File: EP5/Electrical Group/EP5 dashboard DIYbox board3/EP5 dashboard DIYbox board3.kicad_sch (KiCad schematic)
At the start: 9 parts, among them J1 suspension left, J2 suspension right, J3 MCU, J4 wheel left, J5 wheel right

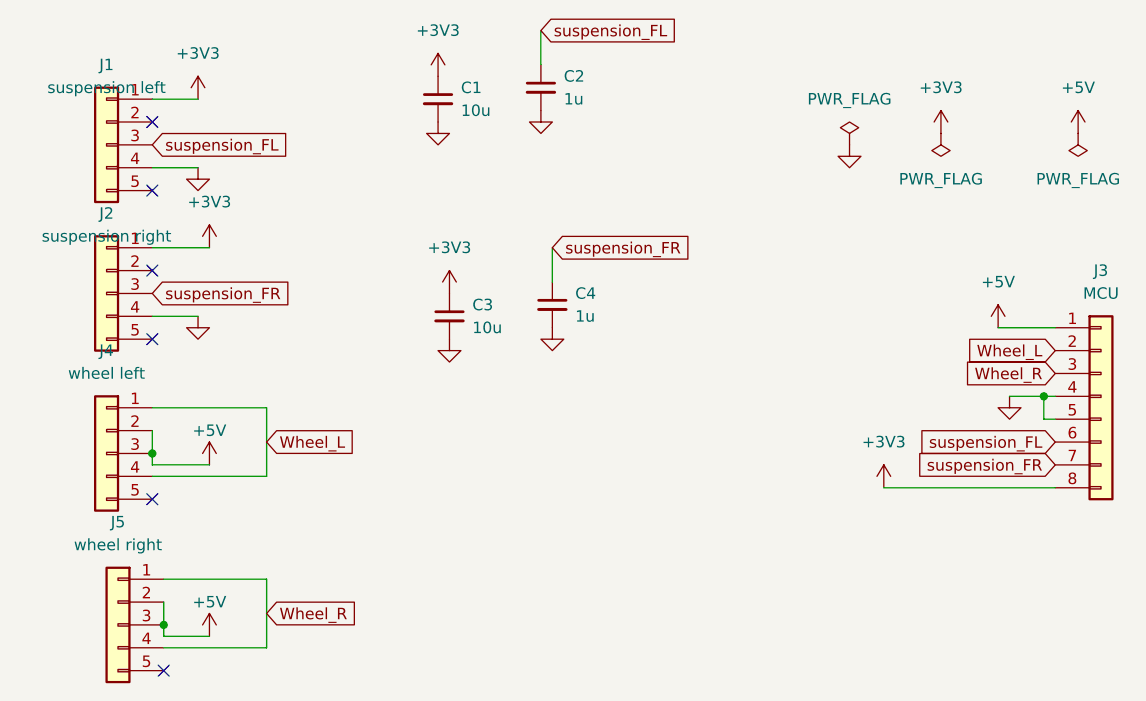
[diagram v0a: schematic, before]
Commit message: update dashboard boards after Tsou's review
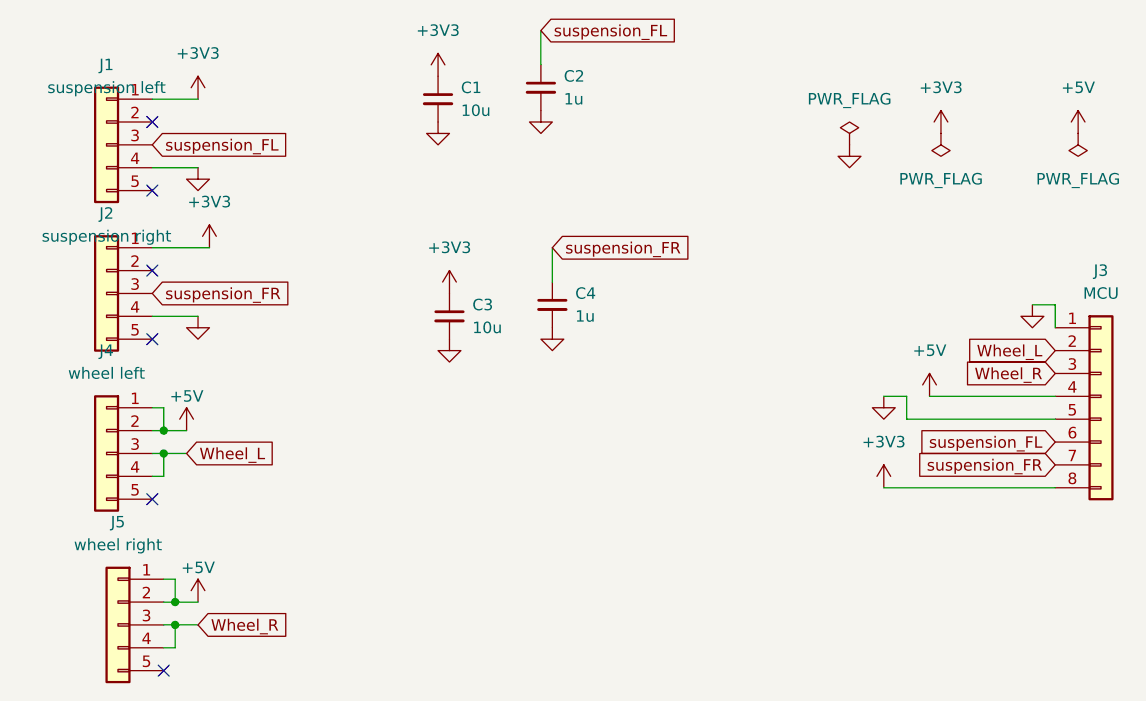
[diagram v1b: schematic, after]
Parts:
- C1, C2, C3, C4: footprint Capacitor_SMD:C_0805_2012Metric -> Capacitor_Tantalum_SMD:CP_EIA-3528-15_AVX-H_Pad1.50x2.35mm_HandSolder
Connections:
- net +5V: now also J3.4 (Pin_4), J4.1 (Pin_1), J5.1 (Pin_1); no longer J3.1 (Pin_1), J4.3 (Pin_3), J5.3 (Pin_3)
- net GND: now also J3.1 (Pin_1); no longer J3.4 (Pin_4)
- net Wheel_L: now also J4.3 (Pin_3); no longer J4.1 (Pin_1)
- net Wheel_R: now also J5.3 (Pin_3); no longer J5.1 (Pin_1)

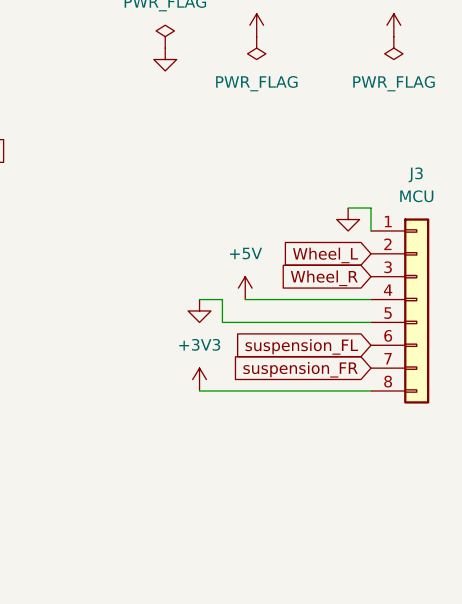
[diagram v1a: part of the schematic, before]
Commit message: update all boards after Tsou's second review
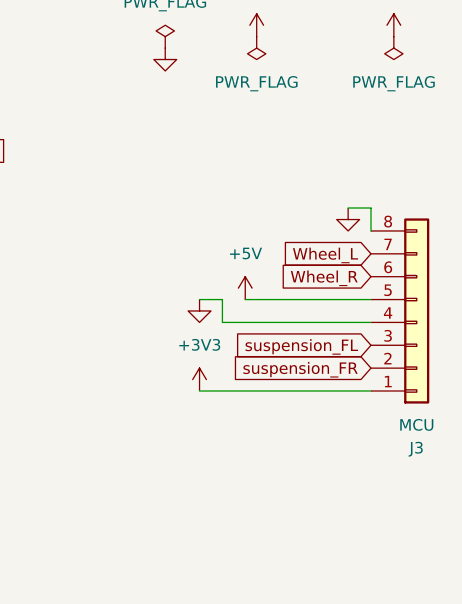
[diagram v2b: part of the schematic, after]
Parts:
- C1, C2, C3, C4: footprint Capacitor_Tantalum_SMD:CP_EIA-3528-15_AVX-H_Pad1.50x2.35mm_HandSolder -> Capacitor_SMD:C_0805_2012Metric
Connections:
- net +3V3: now also J3.1 (Pin_1); no longer J3.8 (Pin_8)
- net +5V: now also J3.5 (Pin_5); no longer J3.4 (Pin_4)
- net GND: now also J3.4 (Pin_4), J3.8 (Pin_8); no longer J3.1 (Pin_1), J3.5 (Pin_5)
- net Wheel_L: now also J3.7 (Pin_7); no longer J3.2 (Pin_2)
- net Wheel_R: now also J3.6 (Pin_6); no longer J3.3 (Pin_3)
- net suspension_FL: now also J3.3 (Pin_3); no longer J3.6 (Pin_6)
- net suspension_FR: now also J3.2 (Pin_2); no longer J3.7 (Pin_7)

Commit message: update dashboard board 3 to V2.0 due to box design change
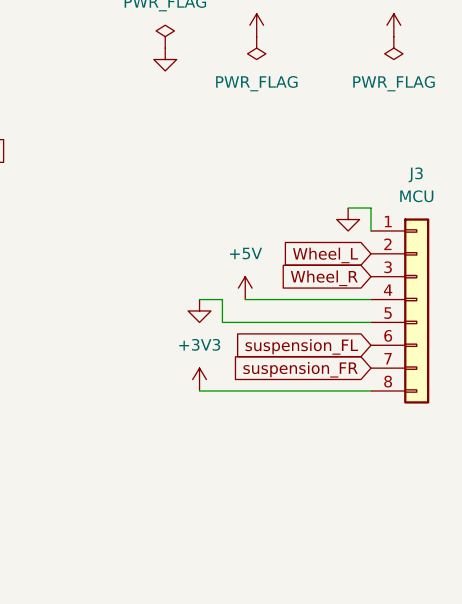
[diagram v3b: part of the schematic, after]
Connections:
- net +3V3: now also J3.8 (Pin_8); no longer J3.1 (Pin_1)
- net +5V: now also J3.4 (Pin_4); no longer J3.5 (Pin_5)
- net GND: now also J3.1 (Pin_1), J3.5 (Pin_5); no longer J3.4 (Pin_4), J3.8 (Pin_8)
- net Wheel_L: now also J3.2 (Pin_2); no longer J3.7 (Pin_7)
- net Wheel_R: now also J3.3 (Pin_3); no longer J3.6 (Pin_6)
- net suspension_FL: now also J3.6 (Pin_6); no longer J3.3 (Pin_3)
- net suspension_FR: now also J3.7 (Pin_7); no longer J3.2 (Pin_2)
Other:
- company: (none) -> NTURacing
- title: (none) -> EP5 dasthboard board3
